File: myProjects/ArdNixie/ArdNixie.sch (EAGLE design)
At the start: 25 parts, among them IC1 74141, IC4 Anode Driver, IC5 SPARKRTC, P1 TRIMPOT, X1 22-23-2021, X2 22-23-2021, X5 Seconds

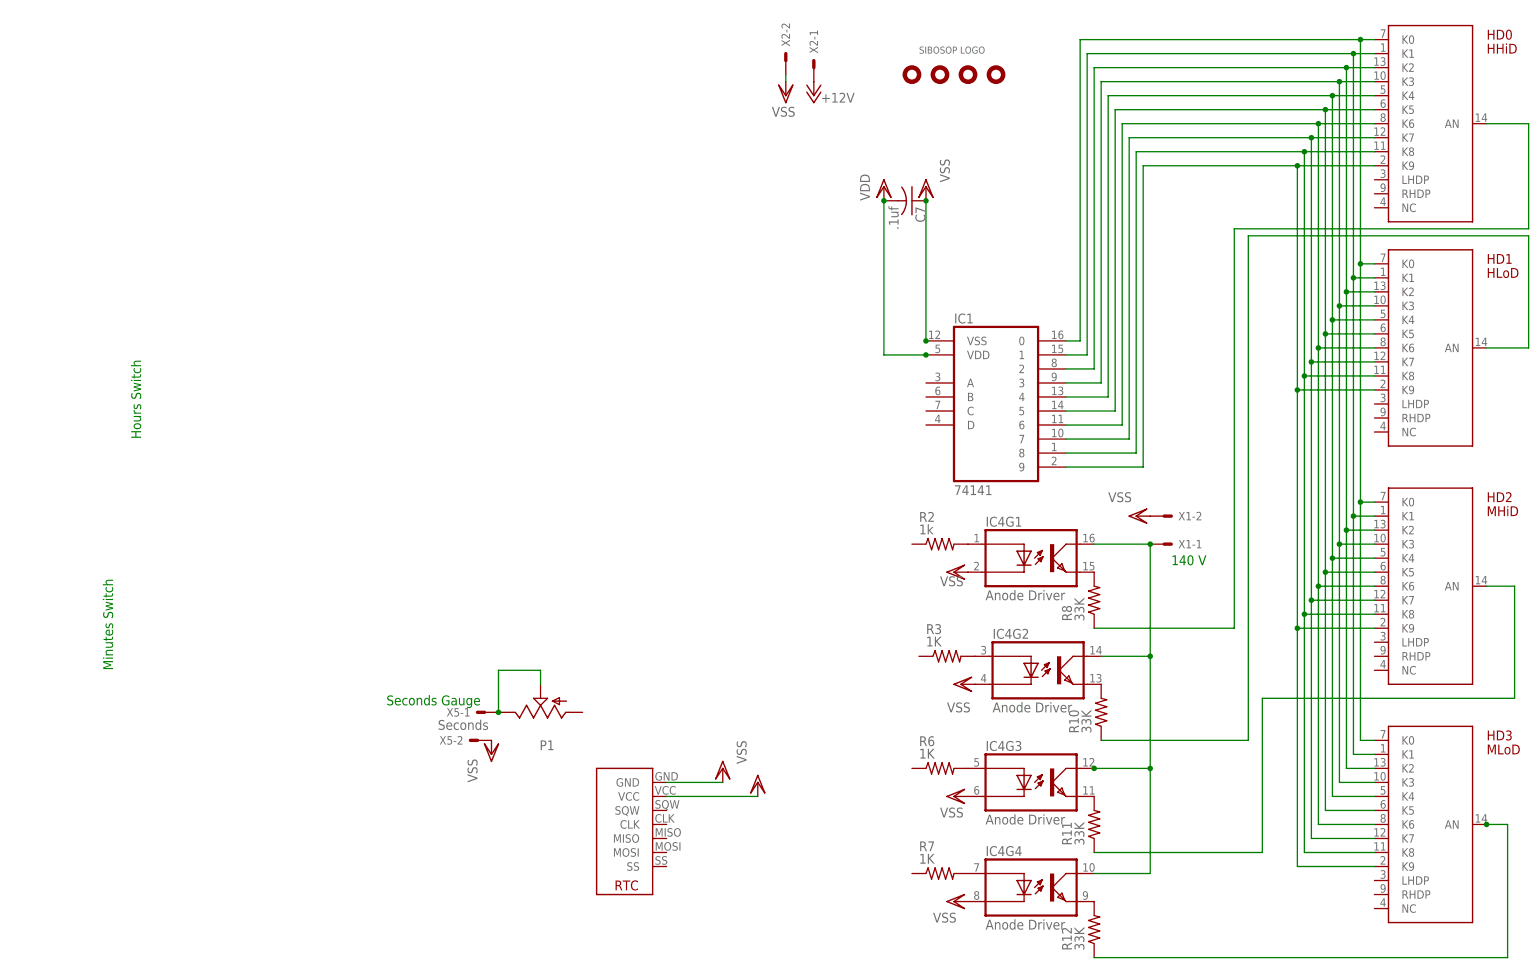
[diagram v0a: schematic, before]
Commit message: finished premil board layout for ardnixie
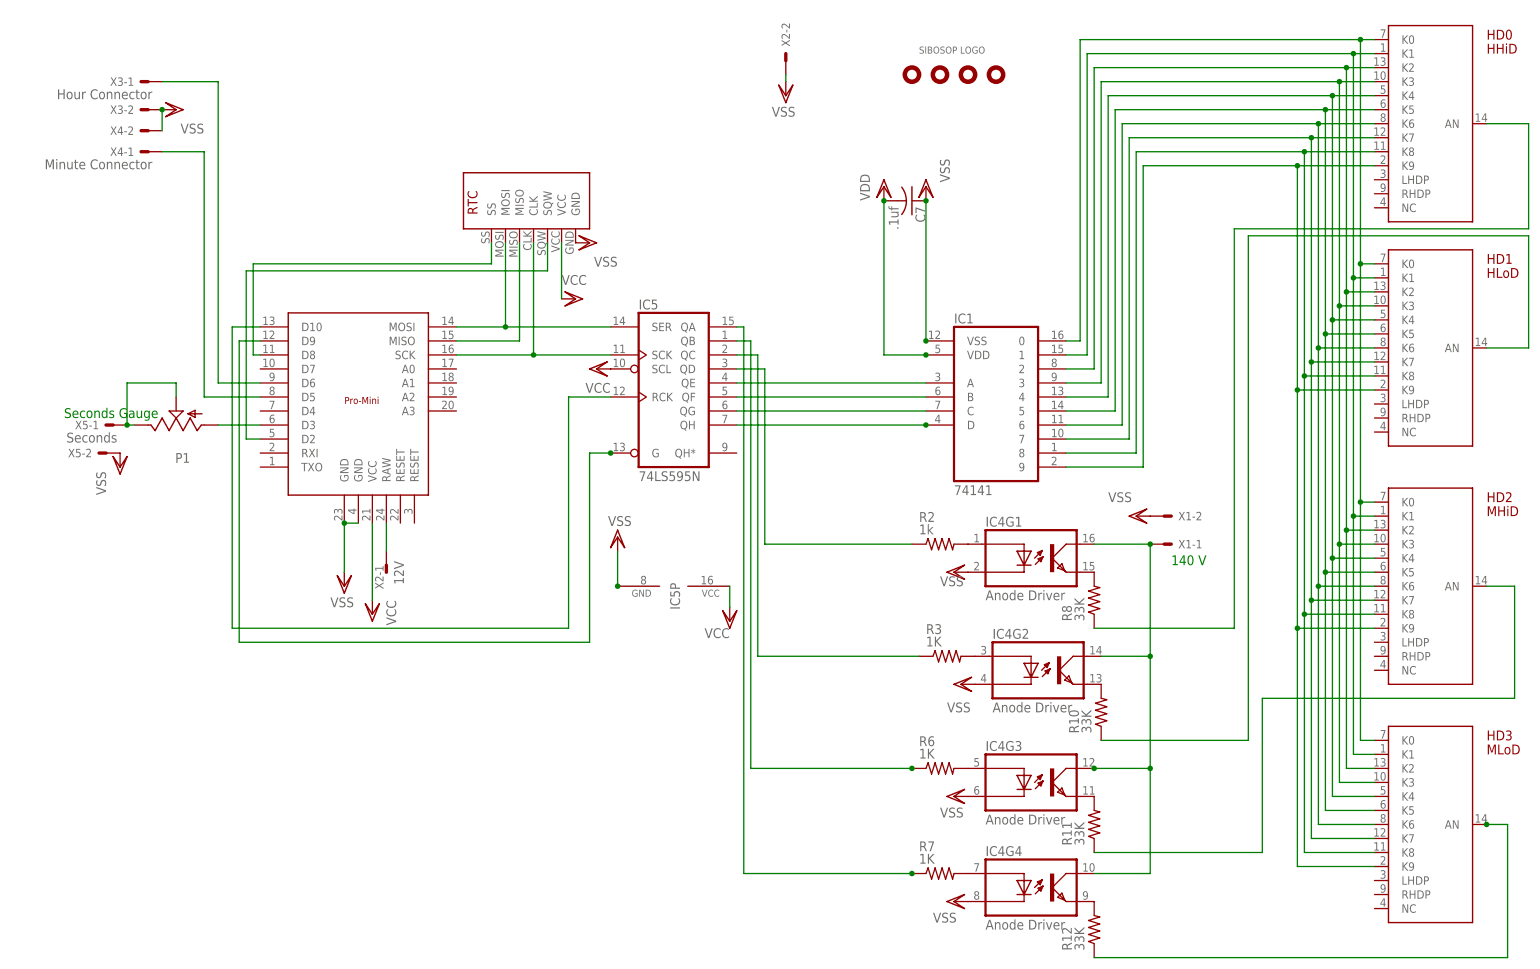
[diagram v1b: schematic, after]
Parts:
- added IC2: PRO-MINI, sibosop:PRO-MINI
- added IC3: SPARKRTC, sibosop:SPARKRTC
- added X3: Hour Connector, sibosop-con-molex:22-23-2021
- added X4: Minute Connector, sibosop-con-molex:22-23-2021
- IC5: value SPARKRTC -> 74LS595N; device sibosop:SPARKRTC -> 74xx-us:74LS595N
- X2: value 22-23-2021 -> 12V
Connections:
- removed net +12V: X2-1.S
- new net N$1: IC5A.QA, R7.1
- new net N$17: IC1.C, IC5A.QG
- new net N$18: IC1.D, IC5A.QH
- new net N$19: IC2.RAW, X2-1.S
- new net N$2: IC5A.QB, R6.1
- new net N$20: IC2.D8, IC3.SS
- new net N$22: IC2.SCK, IC3.CLK, IC5A.SCK
- new net N$23: IC2.MISO, IC3.MISO
- new net N$27: IC2.MOSI, IC3.MOSI, IC5A.SER
- new net N$28: IC2.D2, IC3.SQW
- new net N$29: IC2.D9, IC5A.G
- new net N$3: IC5A.QC, R3.1
- new net N$30: IC2.D10, IC5A.RCK
- new net N$31: IC2.D3, P1.A
- new net N$34: IC2.D5, X4-1.S
- new net N$4: IC5A.QD, R2.1
- new net N$43: IC2.D6, X3-1.S
- new net N$5: IC1.A, IC5A.QE
- new net N$6: IC1.B, IC5A.QF
- net VDD: now also IC2.VCC, IC3.VCC, IC5A.SCL, IC5P.VCC; no longer IC5.VCC
- net VSS: now also IC2.GND@1, IC2.GND@2, IC3.GND, IC5P.GND, X3-2.S, X4-2.S; no longer IC5.GND
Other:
- note removed: "Hours Switch"
- note removed: "Minutes Switch"
- moved on the sheet: P1, X2-1, X5-1, X5-2

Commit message: finished first board design for ArdNixie
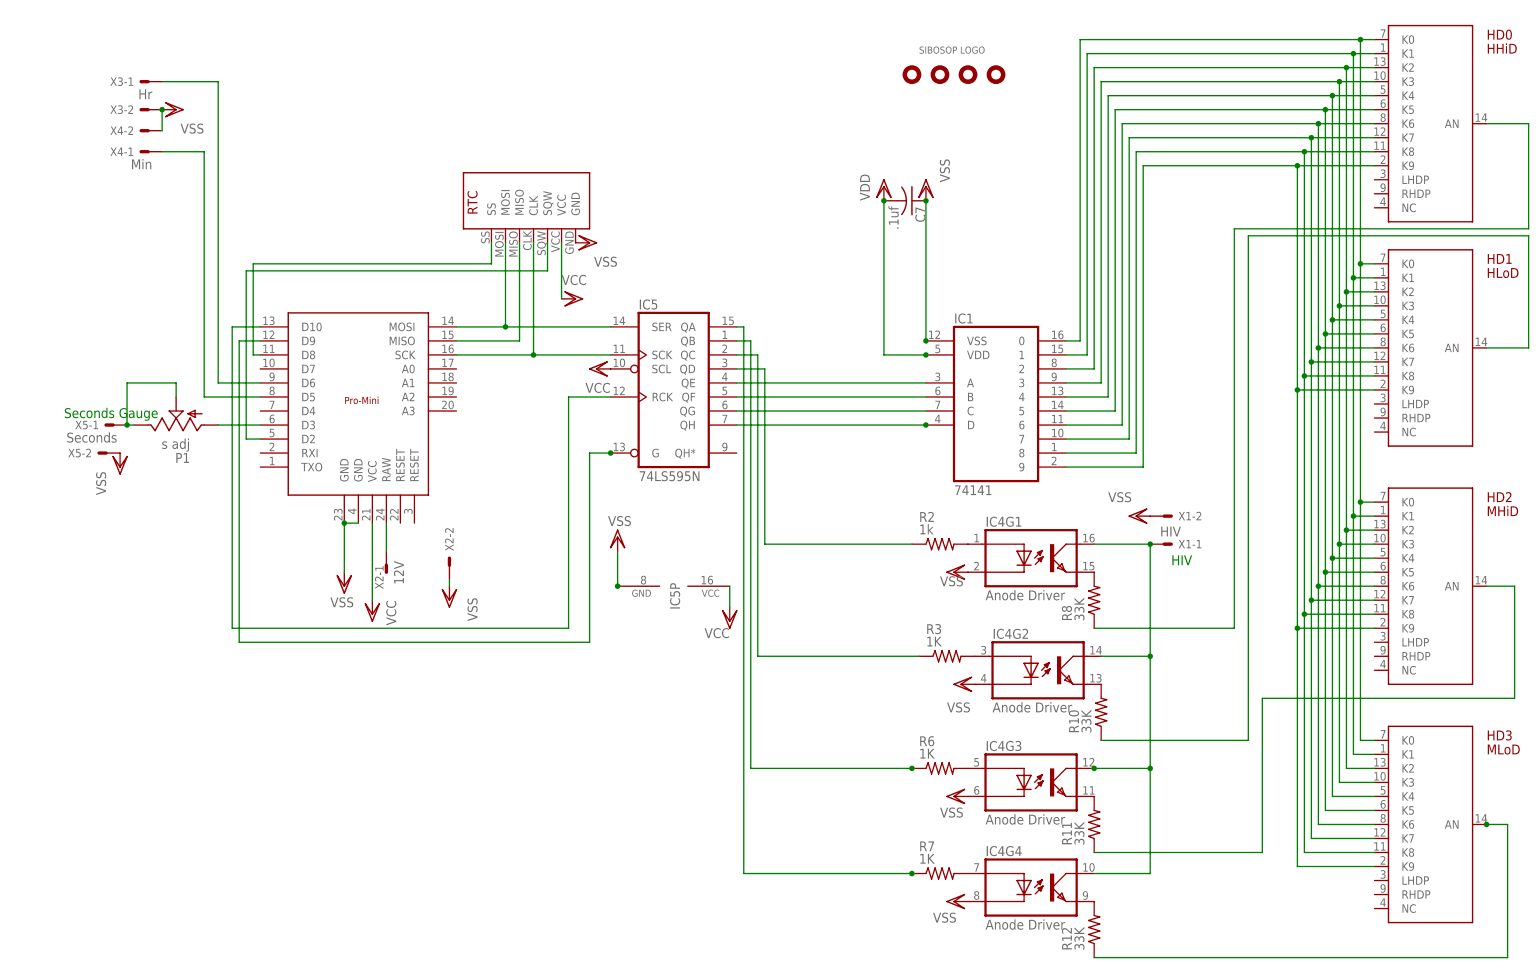
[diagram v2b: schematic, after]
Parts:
- P1: value TRIMPOT -> s adj
- X1: value 22-23-2021 -> HIV
- X3: value Hour Connector -> Hr
- X4: value Minute Connector -> Min
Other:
- note added: "HIV"
- note removed: "140 V"
- moved on the sheet: X2-2
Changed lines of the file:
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@@
 <setting verticaltext="up"/>
 </settings>
-<grid distance="0.05" unitdist="inch" unit="inch" style="lines" multiple="1" display="no" altdistance="0.01" altunitdist="inch" altunit="inch"/>
+<grid distance="0.1" unitdist="inch" unit="inch" style="lines" multiple="1" display="no" altdistance="0.01" altunitdist="inch" altunit="inch"/>
 <layers>
 <layer number="1" name="Top" color="4" fill="1" visible="no" active="no"/>
@@
 <part name="R6" library="rcl" deviceset="R-US_" device="0204/2V" value="1K"/>
 <part name="R7" library="rcl" deviceset="R-US_" device="0204/2V" value="1K"/>
-<part name="X1" library="sibosop-con-molex" deviceset="22-23-2021" device="" value=""/>
+<part name="X1" library="sibosop-con-molex" deviceset="22-23-2021" device="" value="HIV"/>
 <part name="VSS12" library="supply1" deviceset="VSS" device=""/>
 <part name="R8" library="rcl" deviceset="R-US_" device="0204/2V" value="33K"/>
@@
 <part name="R12" library="rcl" deviceset="R-US_" device="0204/2V" value="33K"/>
 <part name="X2" library="sibosop-con-molex" deviceset="22-23-2021" device="" value="12V"/>
-<part name="P1" library="sibosop" deviceset="TRIMPOT" device="" value=""/>
+<part name="P1" library="sibosop" deviceset="TRIMPOT" device="" value="s adj"/>
 <part name="X5" library="sibosop-con-molex" deviceset="22-23-2021" device="" value="Seconds"/>
 <part name="VSS8" library="supply1" deviceset="VSS" device=""/>
@@
 <part name="VCC2" library="supply1" deviceset="VDD" device="" value="VCC"/>
 <part name="VCC3" library="supply1" deviceset="VDD" device="" value="VCC"/>
-<part name="X3" library="sibosop-con-molex" deviceset="22-23-2021" device="" value="Hour Connector"/>
-<part name="X4" library="sibosop-con-molex" deviceset="22-23-2021" device="" value="Minute Connector"/>
+<part name="X3" library="sibosop-con-molex" deviceset="22-23-2021" device="" value="Hr"/>
+<part name="X4" library="sibosop-con-molex" deviceset="22-23-2021" device="" value="Min"/>
 <part name="VSS4" library="supply1" deviceset="VSS" device=""/>
 <part name="VSS6" library="supply1" deviceset="VSS" device=""/>
@@
 <plain>
 <text x="-184.15" y="36.83" size="1.778" layer="91">Seconds Gauge</text>
-<text x="16.51" y="10.16" size="1.778" layer="91">140 V</text>
+<text x="16.51" y="10.16" size="1.778" layer="91">HIV</text>
 </plain>
 <instances>
 <instance part="U$1" gate="G$1" x="-20.32" y="99.06"/>
 <instance part="U$2" gate="G$1" x="-25.4" y="99.06"/>
-<instance part="VSS15" gate="G$1" x="-53.34" y="95.25" smashed="yes">
-<attribute name="VALUE" x="-55.88" y="91.44" size="1.778" layer="96"/>
+<instance part="VSS15" gate="G$1" x="-114.3" y="3.81" smashed="yes">
+<attribute name="VALUE" x="-109.22" y="0" size="1.778" layer="96" rot="R90"/>
 </instance>
 <instance part="U$5" gate="G$1" x="-30.48" y="99.06"/>
@@
 <attribute name="VALUE" x="-124.333" y="10.922" size="1.778" layer="96" rot="R270"/>
 </instance>
-<instance part="X2" gate="-2" x="-53.34" y="101.6" rot="R90"/>
+<instance part="X2" gate="-2" x="-114.3" y="10.16" rot="R90"/>
 <instance part="P1" gate="G$1" x="-163.83" y="35.56" rot="R90"/>
 <instance part="X5" gate="-1" x="-175.26" y="35.56" rot="R180"/>
@@
 </segment>
 <segment>
-<wire x1="-53.34" y1="99.06" x2="-53.34" y2="97.79" width="0.1524" layer="91"/>
+<wire x1="-114.3" y1="7.62" x2="-114.3" y2="6.35" width="0.1524" layer="91"/>
 <pinref part="VSS15" gate="G$1" pin="VSS"/>
 <pinref part="X2" gate="-2" pin="S"/>
